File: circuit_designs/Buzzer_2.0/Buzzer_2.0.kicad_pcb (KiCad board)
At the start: 2 copper layers, 59 x 39.5 mm, 10 parts, among them U1 NE555P

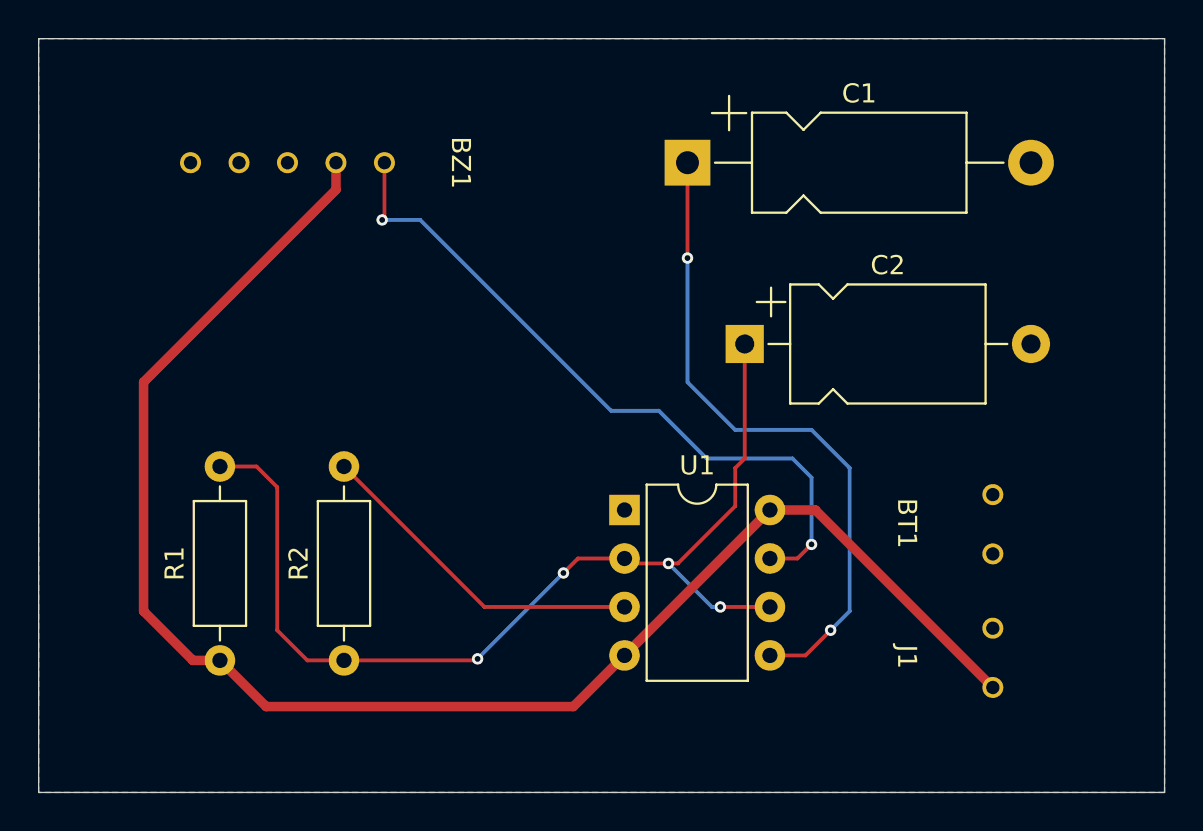
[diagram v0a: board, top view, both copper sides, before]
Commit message: fixed buzzer circuit - removed positive net plane
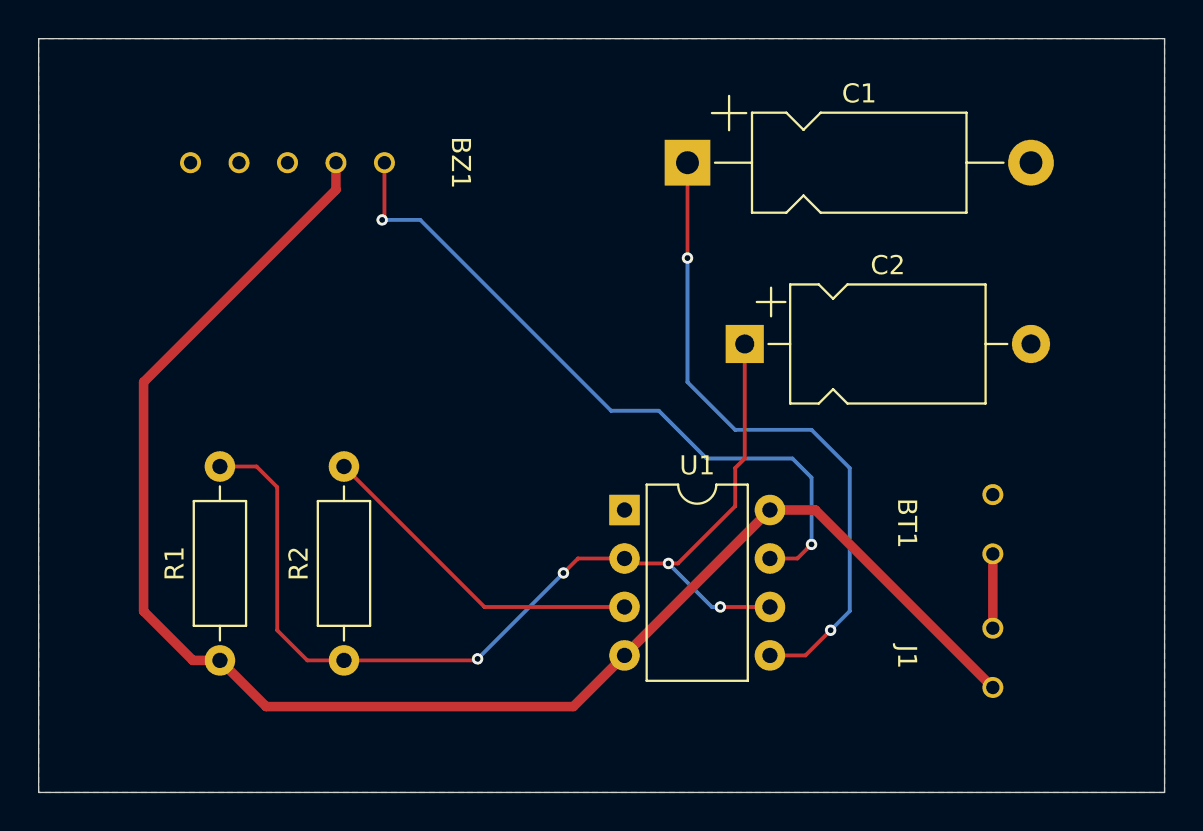
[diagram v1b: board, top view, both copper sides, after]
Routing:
- net 5V: track 0.00 -> 3.89 mm
- removed copper zone on F.Cu, net 5V
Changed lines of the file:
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@@
 		(tags "THT DIP DIL PDIP 2.54mm 7.62mm 300mil")
 		(property "Reference" "U1"
-			(at 3.81 -2.33 360)
+			(at 3.81 -2.33 0)
 			(layer "F.SilkS")
 			(effects
@@
 		)
 		(property "Value" "NE555P"
-			(at 3.81 9.95 360)
+			(at 3.81 9.95 0)
 			(layer "F.Fab")
 			(effects
@@
 		)
 		(fp_text user "${REFERENCE}"
-			(at 3.81 3.81 360)
+			(at 3.81 3.81 0)
 			(layer "F.Fab")
 			(effects
@@
 		(net 6)
 	)
+	(segment
+		(start 160.5 93)
+		(end 160.5 96.8925)
+		(width 0.5)
+		(layer "F.Cu")
+		(net 7)
+	)
 	(zone
-		(net 7)
-		(net_name "5V")
-		(layer "F.Cu")
-		(hatch edge 0.5)
-		(connect_pads
-			(clearance 0.5)
-		)
-		(min_thickness 0.25)
-		(filled_areas_thickness no)
-		(fill yes
-			(thermal_gap 0.5)
-			(thermal_bridge_width 0.5)
-		)
-		(polygon
-			(pts
-				(xy 110.5 66) (xy 169.5 66) (xy 169.5 105.5) (xy 110.5 105.5)
-			)
-		)
-	)
-	(zone
